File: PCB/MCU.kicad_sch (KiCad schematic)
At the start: 37 parts, among them J1 SWD, J2 VIK Keyboard, J3 OLED Breakout, J4 OLED JST, J9 TC2030-NL, U1 ZD25WQ32CEIGR, U2 RP2040, U3 SN74AHCT1G125, U4 REF3033, Y1 12MHz

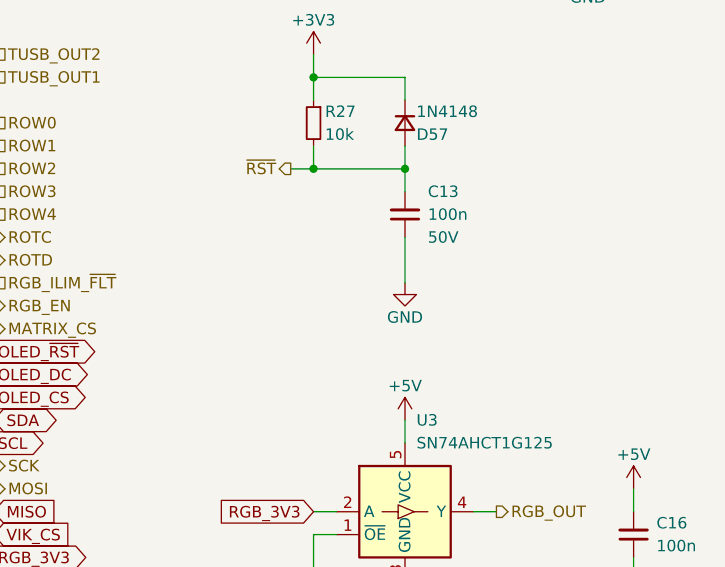
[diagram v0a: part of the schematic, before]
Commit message: 30/07/2023 update
Added VIK keyboard certification card. Added USB connector back to PCB, but left the two buttons on a separate daughterboard. Modified case to accommodate large VIK module.
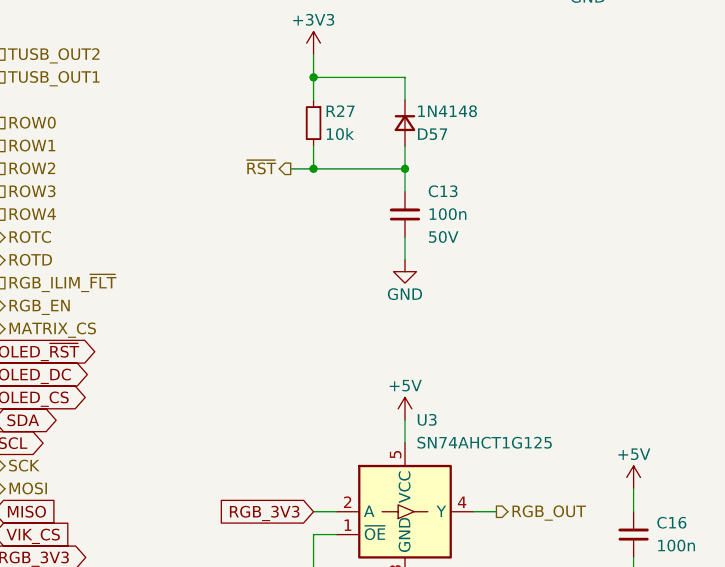
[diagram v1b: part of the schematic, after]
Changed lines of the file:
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@@
   (title_block
     (title "Honeydew unified split ergonomic keyboard")
-    (date "2023-07-29")
+    (date "2023-07-30")
     (rev "V3.0")
     (company "Created by Ariamelon (https://github.com/Ariamelon/Honeydew/)")
@@
     (stroke (width 0) (type default))
   )
-  (wire (pts (xy 210.82 68.58) (xy 210.82 73.66))
+  (wire (pts (xy 210.82 68.58) (xy 210.82 71.12))
     (stroke (width 0) (type default))
   )
@@
     )
   )
-  (symbol (lib_id "power:GND") (at 210.82 73.66 0) (unit 1)
-    (in_bom yes) (on_board yes) (dnp no)
-    (property "Reference" "#PWR038" (at 210.82 80.01 0)
-      (effects (font (size 1.27 1.27)) hide)
-    )
-    (property "Value" "GND" (at 210.82 77.47 0)
-      (effects (font (size 1.27 1.27)))
-    )
-    (property "Footprint" "" (at 210.82 73.66 0)
-      (effects (font (size 1.27 1.27)) hide)
-    )
-    (property "Datasheet" "" (at 210.82 73.66 0)
-      (effects (font (size 1.27 1.27)) hide)
-    )
+  (symbol (lib_id "power:GND") (at 210.82 71.12 0) (unit 1)
+    (in_bom yes) (on_board yes) (dnp no)
+    (property "Reference" "#PWR038" (at 210.82 77.47 0)
+      (effects (font (size 1.27 1.27)) hide)
+    )
+    (property "Value" "GND" (at 210.82 74.93 0)
+      (effects (font (size 1.27 1.27)))
+    )
+    (property "Footprint" "" (at 210.82 71.12 0)
+      (effects (font (size 1.27 1.27)) hide)
+    )
+    (property "Datasheet" "" (at 210.82 71.12 0)
+      (effects (font (size 1.27 1.27)) hide)
+    )

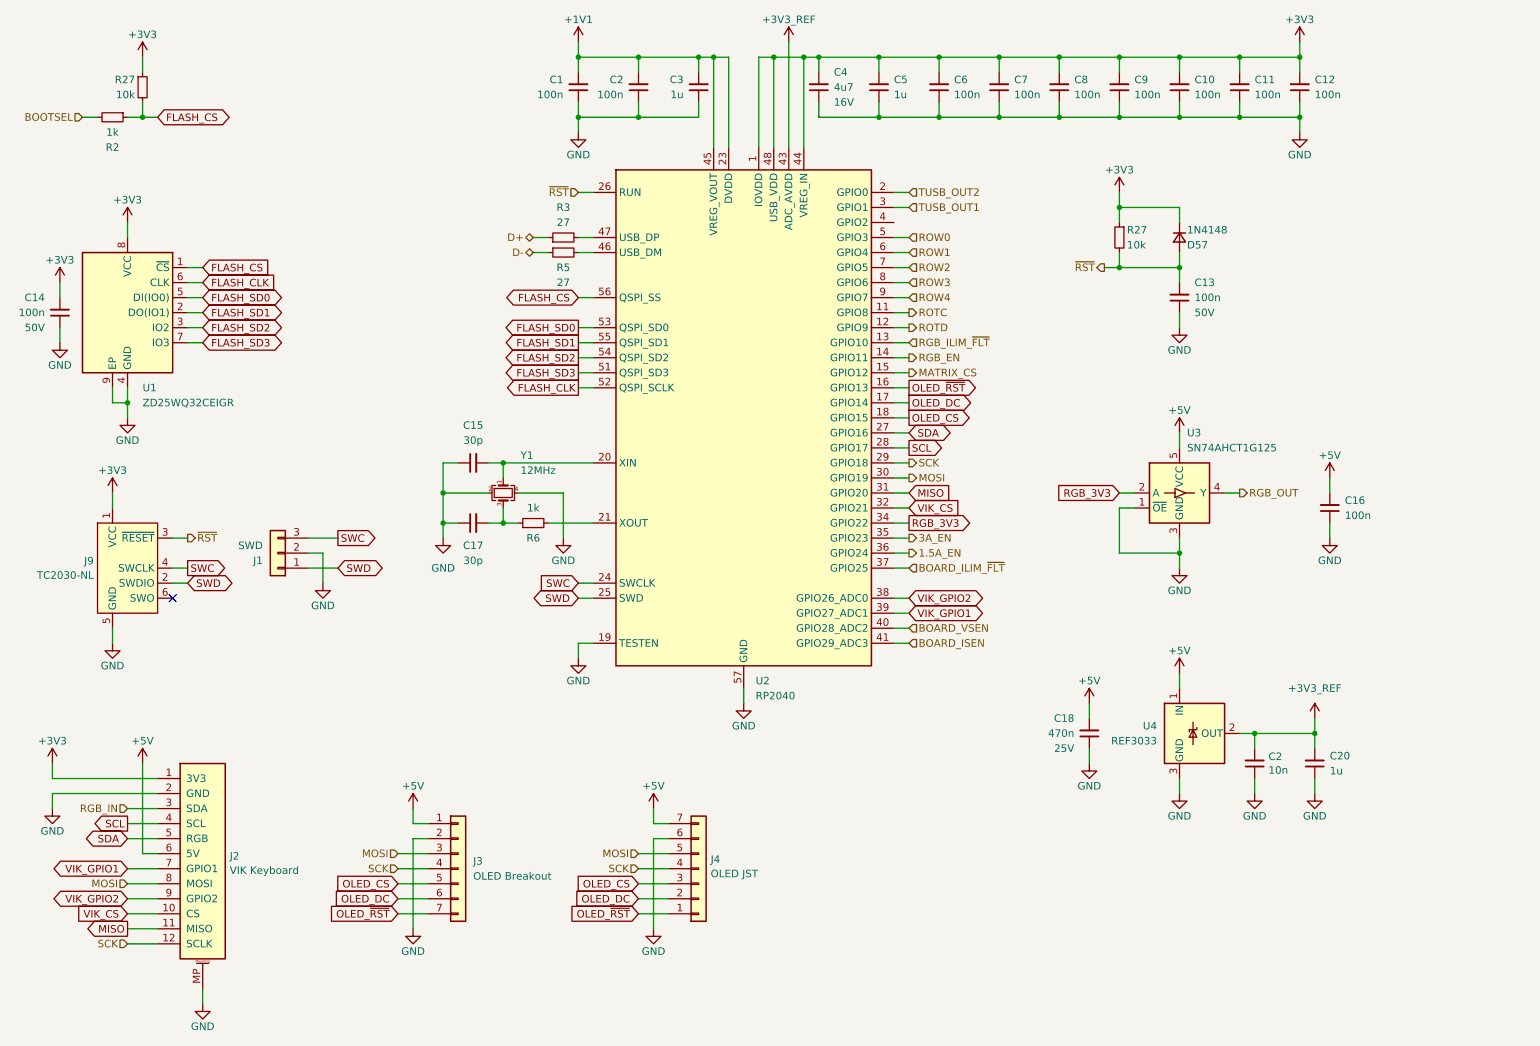
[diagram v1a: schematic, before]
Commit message: 31/07/2023 update
Removed button daughterboard. Reduced size of case and gaskets and added locating features. Added o-ring mounting for the PCB to the bottom case. Added fittings BOM.
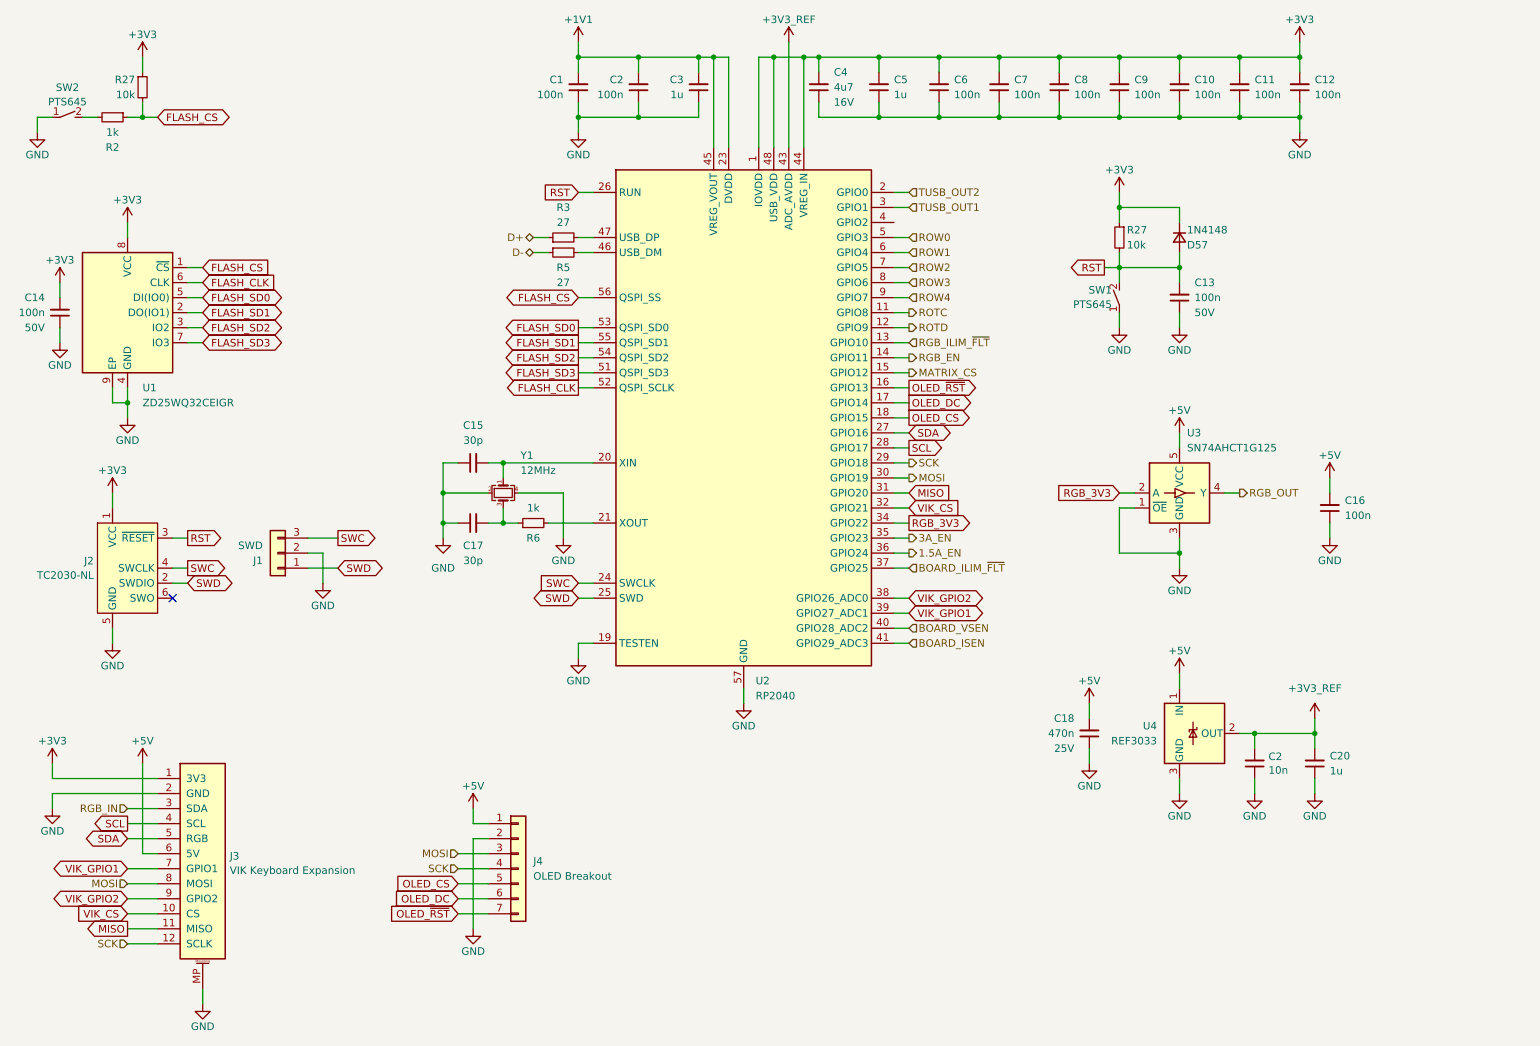
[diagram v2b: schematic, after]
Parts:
- removed J4: OLED JST, Connector_JST:JST_PH_S7B-PH-K_1x07_P2.00mm_Horizontal, symbol Connector_Generic:Conn_01x07
- added SW1, SW2: PTS645, Honeydew:SW_SPST_PTS645, symbol Cantaloupe:SW_SPST_Small
- J3: renamed from J2; value VIK Keyboard -> VIK Keyboard Expansion
- renumbered J9 to J2, J3 to J4
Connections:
- net GND: now also SW1.1 (A), SW2.1 (A)
- net BOOTSEL: no longer names the net of R2.2
- net BOOTSEL: now also SW2.2 (B)
- net ~{RST} renamed RST
- net RST: now also SW1.2 (B)
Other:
- moved on the sheet: J4

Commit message: 04/08/2023 update
Updated SK6812 MINI-E and switch footprints. Changed VIK FFC to FH12. Fixed VIK footprint. Replaced second TPS2595 with AO3401 PFET. Fixed trackpad mount, thumb scroll wheel and scroll wheel mount.
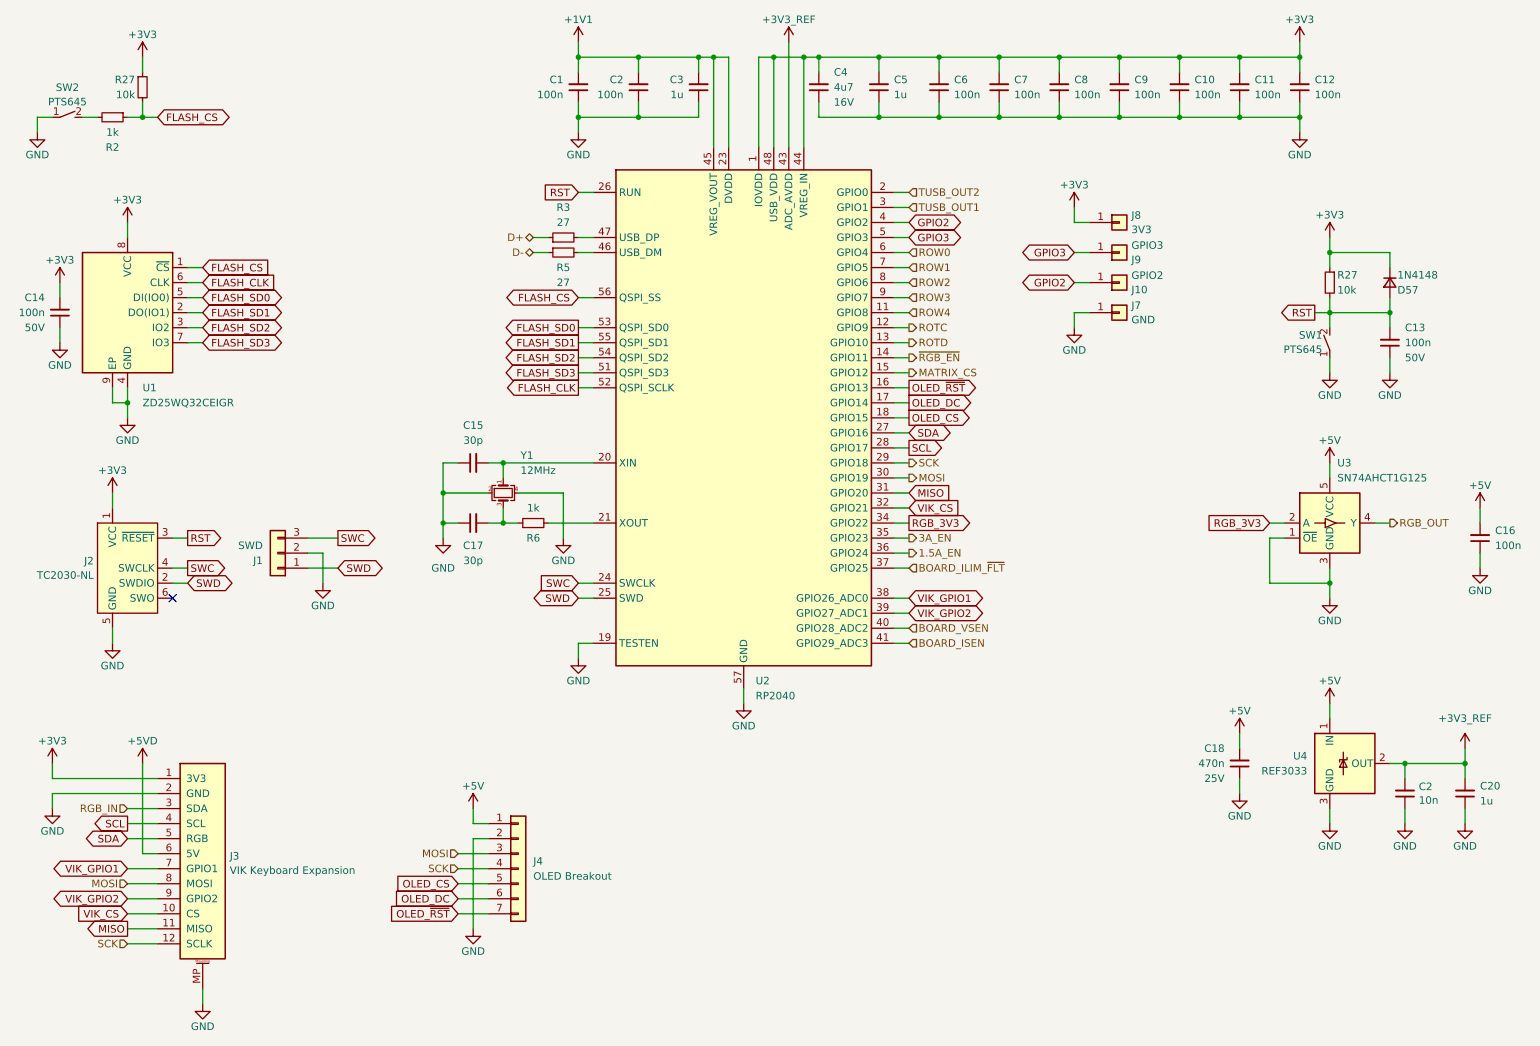
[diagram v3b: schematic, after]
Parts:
- added J10: GPIO2, TestPoint:TestPoint_Pad_D1.5mm, symbol Connector_Generic:Conn_01x01
- added J7: GND, TestPoint:TestPoint_Pad_D1.5mm, symbol Connector_Generic:Conn_01x01
- added J8: 3V3, TestPoint:TestPoint_Pad_D1.5mm, symbol Connector_Generic:Conn_01x01
- added J9: GPIO3, TestPoint:TestPoint_Pad_D1.5mm, symbol Connector_Generic:Conn_01x01
- J3: LCSC C424659 -> C88360
- U4: footprint Package_TO_SOT_SMD:SOT-23 -> Honeydew:SOT-23-3
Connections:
- net RGB_ILIM_~{FLT} is gone; now on net ROTD: U2.13 (GPIO10)
- net +3V3: now also J8.1 (Pin_1)
- net +5V: no longer J3.6 (5V)
- net GND: now also J7.1 (Pin_1)
- net ROTC: now also U2.12 (GPIO9); no longer U2.11 (GPIO8)
- net ROTD: no longer U2.12 (GPIO9)
- net ROW0: now also U2.6 (GPIO4); no longer U2.5 (GPIO3)
- net ROW1: now also U2.7 (GPIO5); no longer U2.6 (GPIO4)
- net ROW2: now also U2.8 (GPIO6); no longer U2.7 (GPIO5)
- net ROW3: now also U2.9 (GPIO7); no longer U2.8 (GPIO6)
- net ROW4: now also U2.11 (GPIO8); no longer U2.9 (GPIO7)
- net VIK_GPIO1: now also U2.38 (GPIO26_ADC0); no longer U2.39 (GPIO27_ADC1)
- net VIK_GPIO2: now also U2.39 (GPIO27_ADC1); no longer U2.38 (GPIO26_ADC0)
- net GPIO2: now reaches U2.4 (GPIO2)
- net GPIO2: now also J10.1 (Pin_1)
- net RGB_EN renamed ~{RGB_EN}
- new net +5VD: J3.6 (5V)
- new net GPIO3: J9.1 (Pin_1), U2.5 (GPIO3)
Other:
- moved on the sheet: C13, C16, C18, C2, C20, D57, R27, SW1, U3, U4

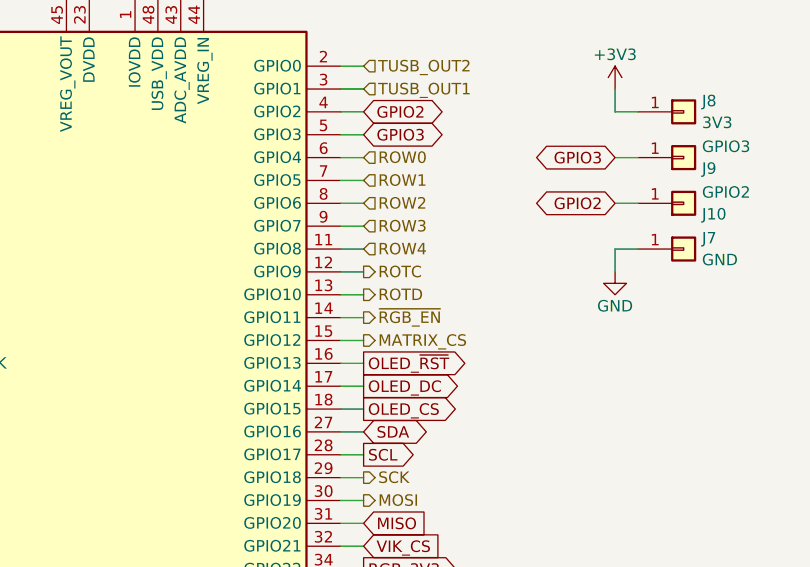
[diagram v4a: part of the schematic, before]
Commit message: 06/08/2023 update
Changed switch footprint back to MX only, as it's too much money to risk on an experimental footprint, and rerouted the relevant traces. Cleaned up footprint library by removing many unused footprints.
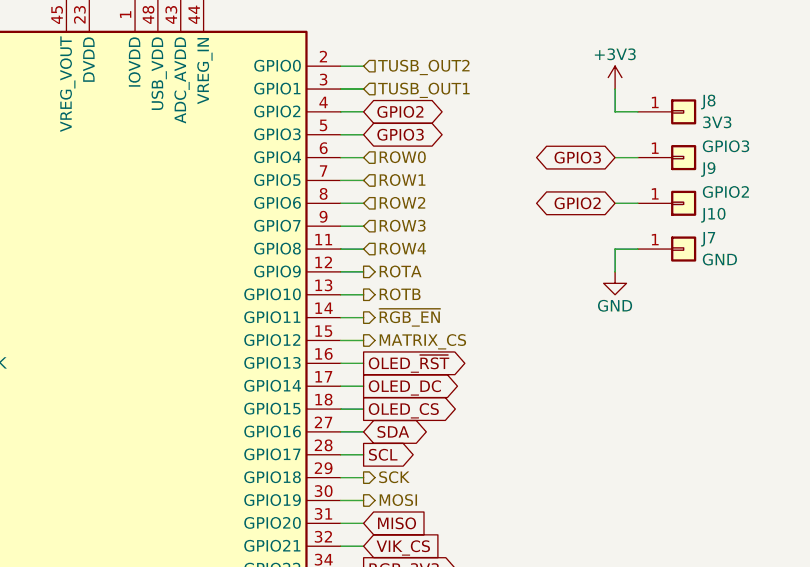
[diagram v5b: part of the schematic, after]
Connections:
- net ROTC renamed ROTA
- net ROTD renamed ROTB
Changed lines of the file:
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@@
   (title_block
     (title "Honeydew unified split ergonomic keyboard")
-    (date "2023-08-05")
+    (date "2023-08-06")
     (rev "V3.0")
     (company "Created by Ariamelon (https://github.com/Ariamelon/Honeydew/)")
@@
     )
   )
-  (hierarchical_label "ROTC" (shape output) (at 165.1 71.12 0) (fields_autoplaced)
+  (hierarchical_label "ROTA" (shape output) (at 165.1 71.12 0) (fields_autoplaced)
     (effects (font (size 1.27 1.27)) (justify left))
   )
@@
     (effects (font (size 1.27 1.27)) (justify left))
   )
-  (hierarchical_label "ROTD" (shape output) (at 165.1 73.66 0) (fields_autoplaced)
-    (effects (font (size 1.27 1.27)) (justify left))
-  )
+  (hierarchical_label "ROTB" (shape output) (at 165.1 73.66 0) (fields_autoplaced)
+    (effects (font (size 1.27 1.27)) (justify left))
+  )
